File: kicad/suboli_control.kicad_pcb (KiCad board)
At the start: 2 copper layers, 125 x 95 mm, 45 parts, among them J1 DC barrel jack panel header 5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, J2 3.5 mm TRS input panel header, J4 3.5 mm TRS headphone panel he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, J5 MA12070 module power, J6 MA12070 module audio in, SW1 DPST power switch panel header, U1 TLE2426ILP

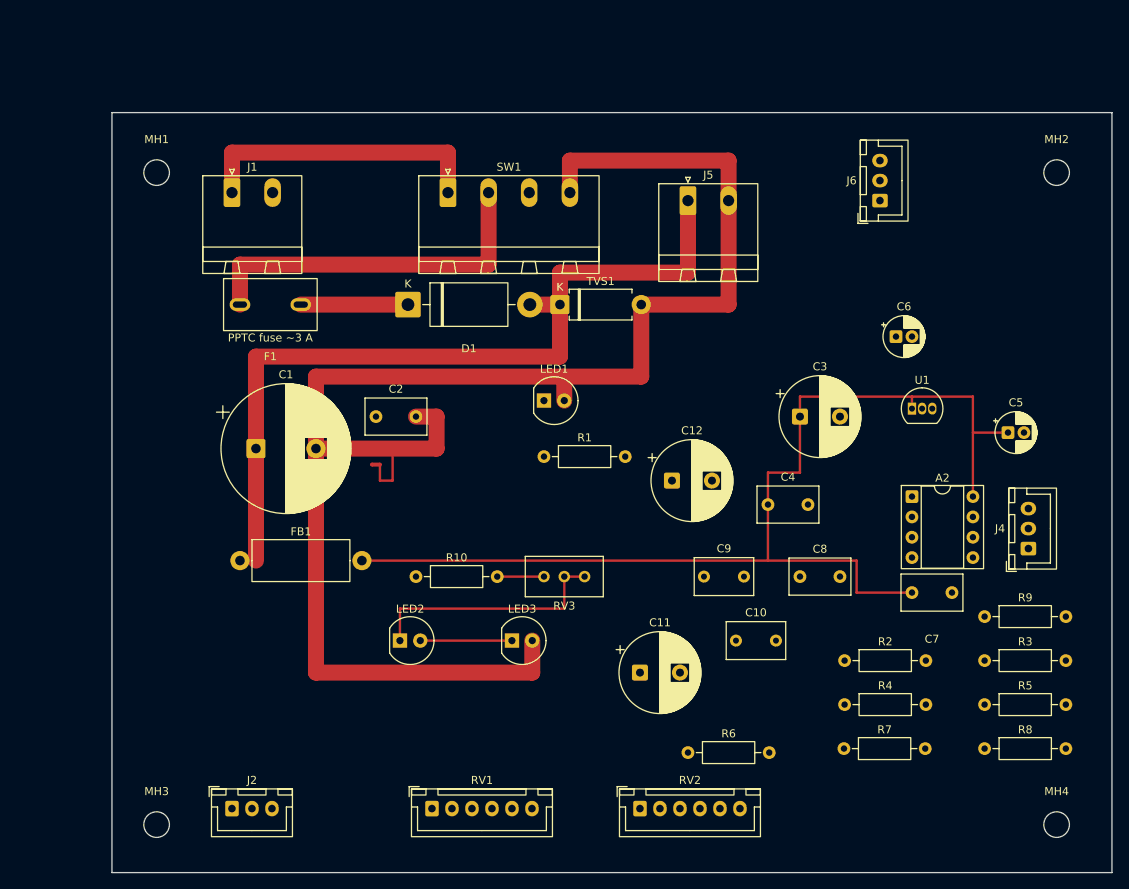
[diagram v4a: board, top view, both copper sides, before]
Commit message: R10: ground pour zones (GND_STAR left / GND_SIG right, split at x70)
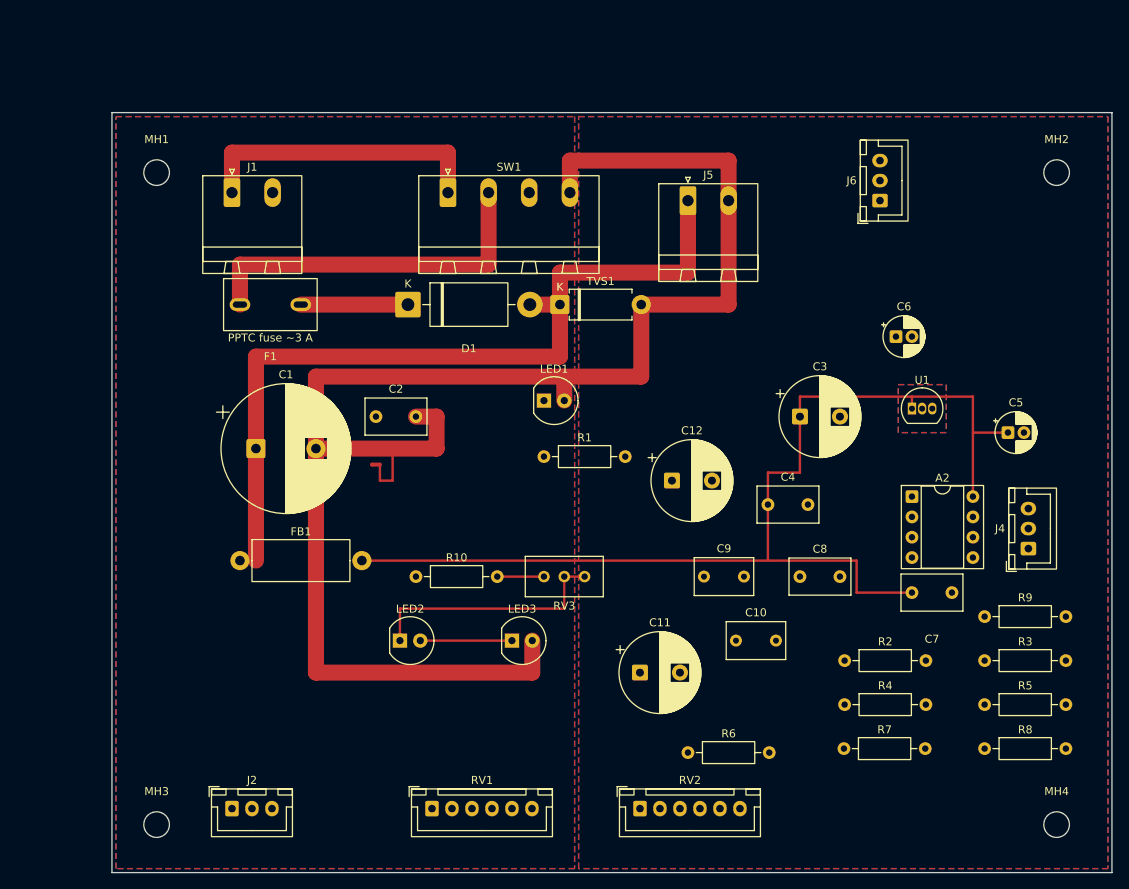
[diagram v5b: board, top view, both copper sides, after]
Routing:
- added copper zone on B.Cu, net /GND_SIG
- added copper zone on F.Cu, net /GND_SIG
- added copper zone on B.Cu, net /GND_STAR
- added copper zone on F.Cu, net /GND_STAR
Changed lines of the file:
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@@
 		(net "/+19V_F")
+	)
+	(zone
+		(net "/GND_STAR")
+		(layers "F.Cu" "B.Cu")
+		(hatch edge 0.5)
+		(connect_pads
+			(clearance 0.2)
+		)
+		(min_thickness 0.5)
+		(fill
+			(thermal_gap 0.2)
+			(thermal_bridge_width 0.5)
+			(island_removal_mode 0)
+		)
+		(polygon
+			(pts
+				(xy 12.42 12.5) (xy 69.75 12.5) (xy 69.75 106.5) (xy 12.42 106.5)
+			)
+		)
+	)
+	(zone
+		(net "/GND_SIG")
+		(layers "F.Cu" "B.Cu")
+		(hatch edge 0.5)
+		(connect_pads
+			(clearance 0.2)
+		)
+		(min_thickness 0.5)
+		(fill
+			(thermal_gap 0.2)
+			(thermal_bridge_width 0.5)
+			(island_removal_mode 0)
+		)
+		(polygon
+			(pts
+				(xy 70.25 12.5) (xy 136.42 12.5) (xy 136.42 106.5) (xy 70.25 106.5)
+			)
+		)
+		(polygon
+			(pts
+				(xy 110.2 46) (xy 116.2 46) (xy 116.2 52) (xy 110.2 52)
+			)
+		)
 	)
 	(embedded_fonts no)

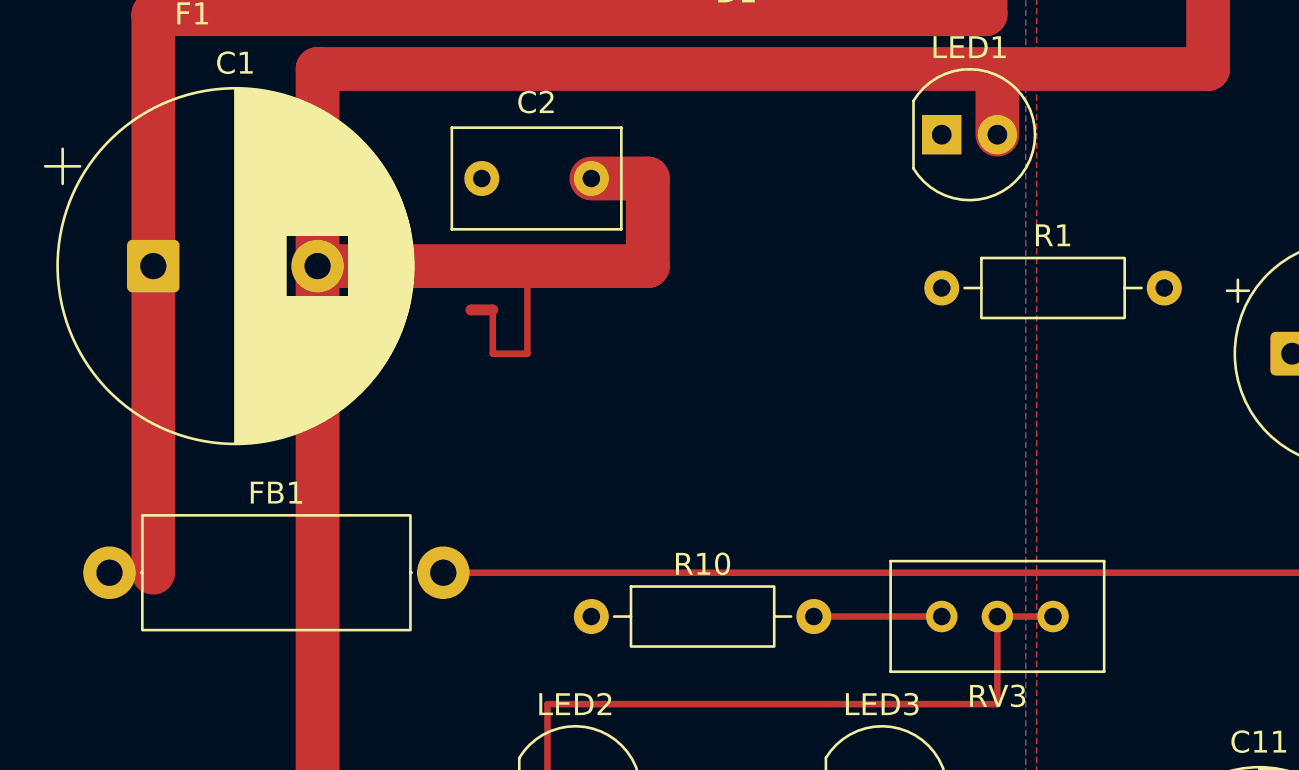
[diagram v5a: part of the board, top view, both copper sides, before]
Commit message: R11: route power leftover branches on B.Cu under ground pour
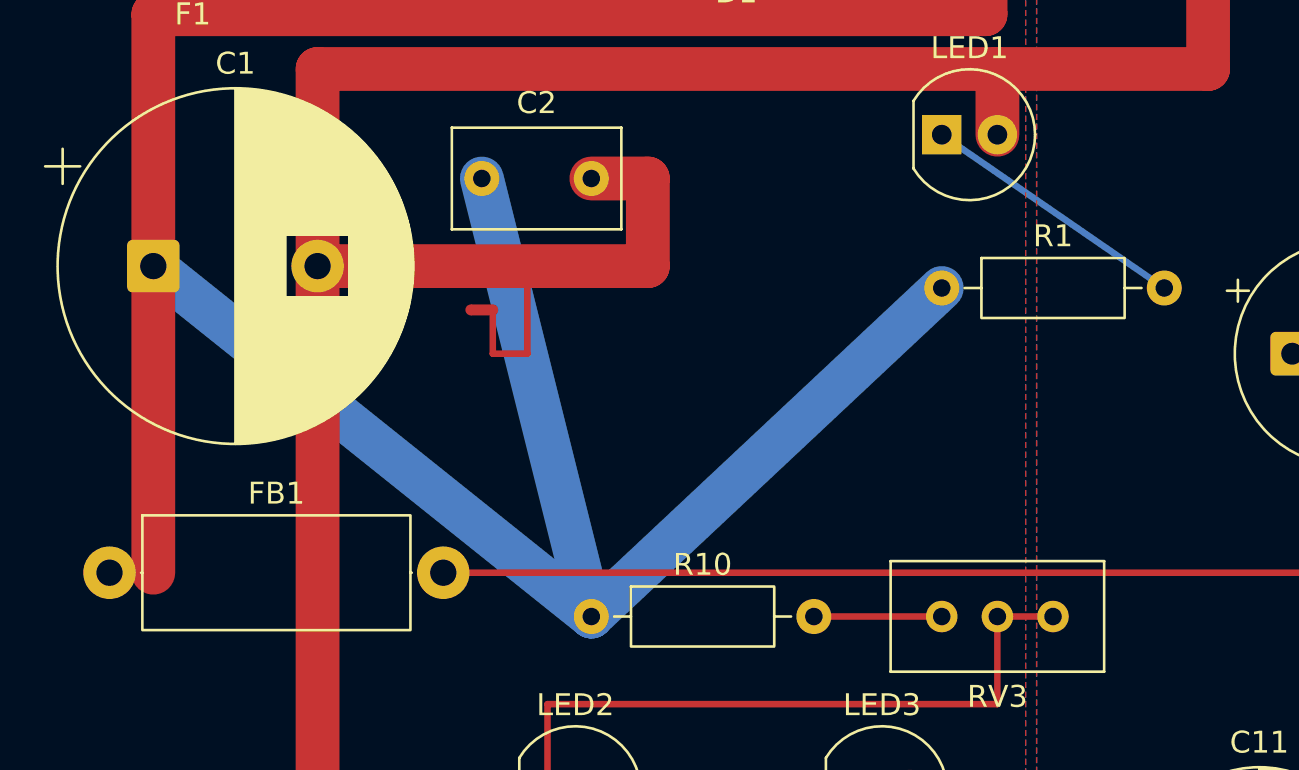
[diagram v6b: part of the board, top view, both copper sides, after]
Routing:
- net /+19V: track 102.8 -> 170.9 mm
- net /PWR_LED_ANODE: track 0.00 -> 12.3 mm
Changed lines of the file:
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@@
+	)
+	(segment
+		(start 49.92 70)
+		(end 65.92 55)
+		(width 2)
+		(layer "B.Cu")
+		(net "/+19V")
+	)
+	(segment
+		(start 29.92 54)
+		(end 49.92 70)
+		(width 2)
+		(layer "B.Cu")
+		(net "/+19V")
+	)
+	(segment
+		(start 49.92 70)
+		(end 44.92 50)
+		(width 2)
+		(layer "B.Cu")
+		(net "/+19V")
 	)
 	(segment
@@
 		(net "/+19V_F")
 	)
-	(zone
-		(net "/GND_STAR")
-		(layers "F.Cu" "B.Cu")
-		(hatch edge 0.5)
-		(connect_pads
-			(clearance 0.2)
-		)
-		(min_thickness 0.5)
-		(fill
-			(thermal_gap 0.2)
-			(thermal_bridge_width 0.5)
-			(island_removal_mode 0)
-		)
-		(polygon
-			(pts
-				(xy 12.42 12.5) (xy 69.75 12.5) (xy 69.75 106.5) (xy 12.42 106.5)
-			)
-		)
+	(segment
+		(start 65.92 48)
+		(end 76.08 55)
+		(width 0.3)
+		(layer "B.Cu")
+		(net "/PWR_LED_ANODE")
 	)
 	(zone
@@
 		)
 		(min_thickness 0.5)
-		(fill
+		(fill yes
 			(thermal_gap 0.2)
 			(thermal_bridge_width 0.5)
@@
 			)
 		)
+	)
+	(zone
+		(net "/GND_STAR")
+		(layers "F.Cu" "B.Cu")
+		(hatch edge 0.5)
+		(connect_pads
+			(clearance 0.2)
+		)
+		(min_thickness 0.5)
+		(fill yes
+			(thermal_gap 0.2)
+			(thermal_bridge_width 0.5)
+			(island_removal_mode 0)
+		)
+		(polygon
+			(pts
+				(xy 12.42 12.5) (xy 69.75 12.5) (xy 69.75 106.5) (xy 12.42 106.5)
+			)
+		)

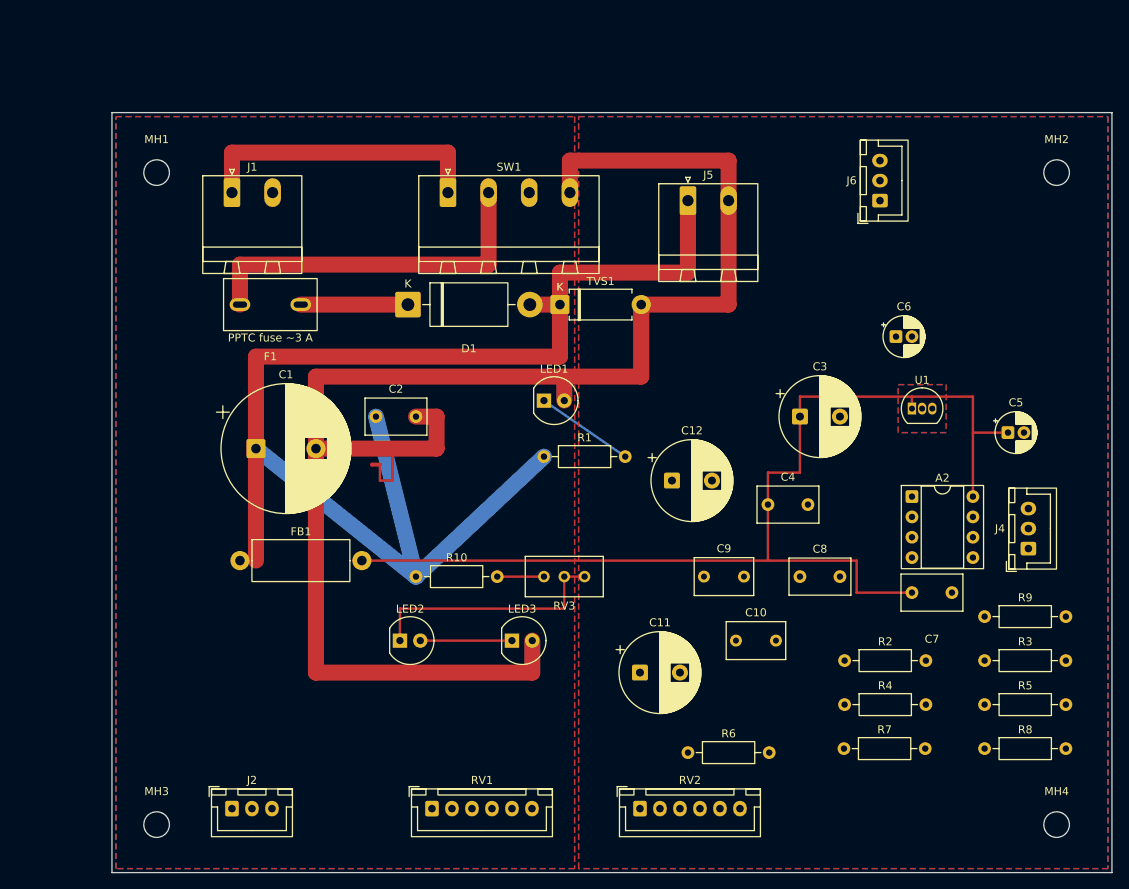
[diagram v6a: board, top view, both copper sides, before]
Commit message: R12: route input + tactile signal nets
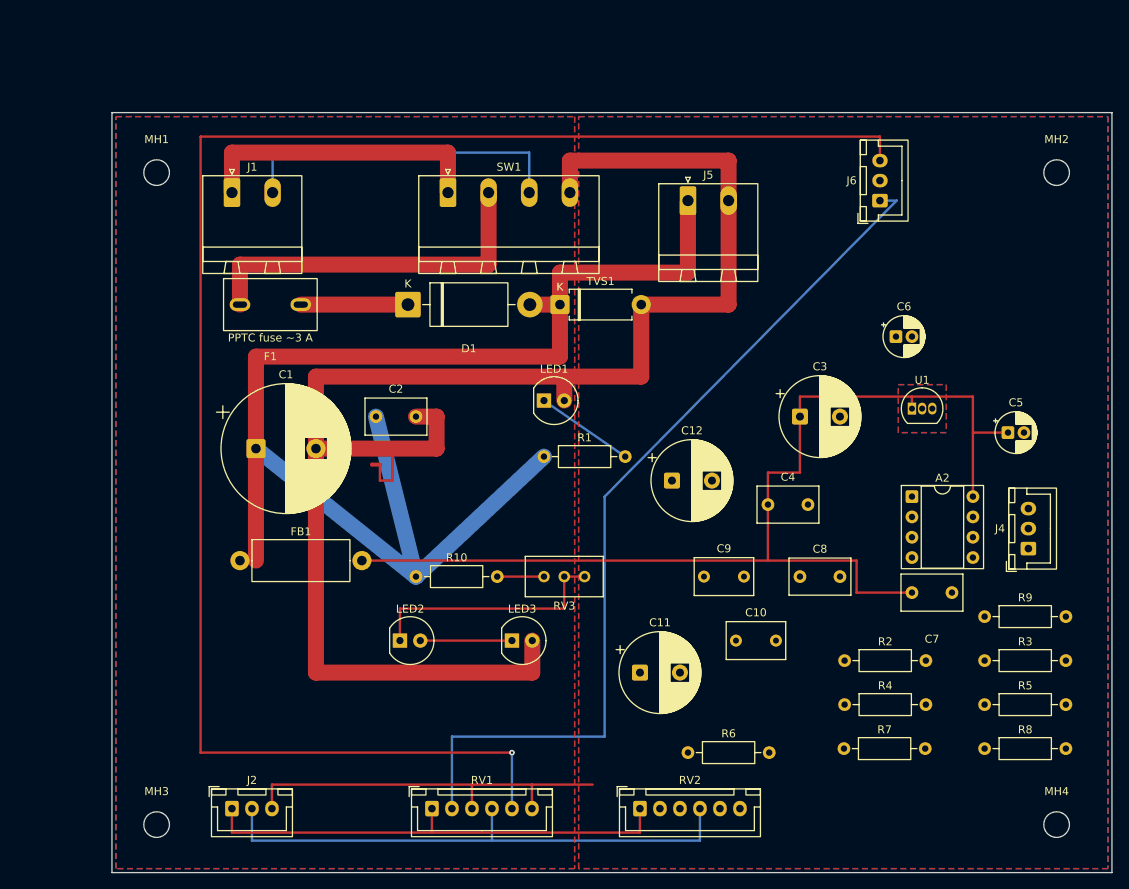
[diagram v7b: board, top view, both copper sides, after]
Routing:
- net /TACT_INR: track 0.00 -> 210.8 mm, vias 0 -> 1
- net /TACT_INL: track 0.00 -> 112.1 mm
- net /IN_R: track 0.00 -> 68.0 mm
- net /IN_L: track 0.00 -> 60.0 mm
- net /GND_SIG: track 0.00 -> 49.1 mm
- net /GND_RAW: track 0.00 -> 42.1 mm
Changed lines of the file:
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@@
+	)
+	(segment
+		(start 56.92 99)
+		(end 56.92 96)
+		(width 0.3)
+		(layer "F.Cu")
+		(net "/GND_SIG")
+	)
+	(segment
+		(start 31.92 99)
+		(end 31.92 96)
+		(width 0.3)
+		(layer "F.Cu")
+		(net "/GND_SIG")
+	)
+	(segment
+		(start 64.42 99)
+		(end 64.42 96)
+		(width 0.3)
+		(layer "F.Cu")
+		(net "/GND_SIG")
+	)
+	(segment
+		(start 31.92 96)
+		(end 72 96)
+		(width 0.3)
+		(layer "F.Cu")
+		(net "/GND_SIG")
 	)
 	(segment
@@
 	)
 	(segment
+		(start 64.08 17)
+		(end 64.08 22)
+		(width 0.3)
+		(layer "B.Cu")
+		(net "/GND_RAW")
+	)
+	(segment
+		(start 32 22)
+		(end 32 17)
+		(width 0.3)
+		(layer "B.Cu")
+		(net "/GND_RAW")
+	)
+	(segment
+		(start 32 17)
+		(end 64.08 17)
+		(width 0.3)
+		(layer "B.Cu")
+		(net "/GND_RAW")
+	)
+	(segment
 		(start 83.92 32)
 		(end 83.92 23)
@@
 	)
 	(segment
+		(start 54.42 99)
+		(end 54.42 90)
+		(width 0.3)
+		(layer "B.Cu")
+		(net "/TACT_INL")
+	)
+	(segment
+		(start 110 23)
+		(end 107.92 23)
+		(width 0.3)
+		(layer "B.Cu")
+		(net "/TACT_INL")
+	)
+	(segment
+		(start 54.42 90)
+		(end 73.5 90)
+		(width 0.3)
+		(layer "B.Cu")
+		(net "/TACT_INL")
+	)
+	(segment
+		(start 73.5 60)
+		(end 110 23)
+		(width 0.3)
+		(layer "B.Cu")
+		(net "/TACT_INL")
+	)
+	(segment
+		(start 73.5 90)
+		(end 73.5 60)
+		(width 0.3)
+		(layer "B.Cu")
+		(net "/TACT_INL")
+	)
+	(segment
+		(start 107.92 15)
+		(end 107.92 18)
+		(width 0.3)
+		(layer "F.Cu")
+		(net "/TACT_INR")
+	)
+	(segment
+		(start 61.92 92)
+		(end 23 92)
+		(width 0.3)
+		(layer "F.Cu")
+		(net "/TACT_INR")
+	)
+	(segment
+		(start 23 92)
+		(end 23 15)
+		(width 0.3)
+		(layer "F.Cu")
+		(net "/TACT_INR")
+	)
+	(segment
+		(start 23 15)
+		(end 107.92 15)
+		(width 0.3)
+		(layer "F.Cu")
+		(net "/TACT_INR")
+	)
+	(via
+		(at 61.92 92)
+		(size 0.7)
+		(drill 0.3)
+		(layers "F.Cu" "B.Cu")
+		(net "/TACT_INR")
+	)
+	(segment
+		(start 61.92 99)
+		(end 61.92 92)
+		(width 0.3)
+		(layer "B.Cu")
+		(net "/TACT_INR")
+	)
+	(segment
+		(start 77.92 99)
+		(end 77.92 102)
+		(width 0.3)
+		(layer "F.Cu")
+		(net "/IN_L")
+	)
+	(segment
+		(start 51.92 99)
+		(end 51.92 102)
+		(width 0.3)
+		(layer "F.Cu")
+		(net "/IN_L")
+	)
+	(segment
+		(start 26.92 99)
+		(end 26.92 102)
+		(width 0.3)
+		(layer "F.Cu")
+		(net "/IN_L")
+	)
+	(segment
+		(start 26.92 102)
+		(end 77.92 102)
+		(width 0.3)
+		(layer "F.Cu")
+		(net "/IN_L")
+	)
+	(segment
+		(start 85.42 99)
+		(end 85.42 103)
+		(width 0.3)
+		(layer "B.Cu")
+		(net "/IN_R")
+	)
+	(segment
+		(start 29.42 103)
+		(end 85.42 103)
+		(width 0.3)
+		(layer "B.Cu")
+		(net "/IN_R")
+	)
+	(segment
+		(start 29.42 99)
+		(end 29.42 103)
+		(width 0.3)
+		(layer "B.Cu")
+		(net "/IN_R")
+	)
+	(segment
+		(start 59.42 99)
+		(end 59.42 103)
+		(width 0.3)
+		(layer "B.Cu")
+		(net "/IN_R")
+	)
+	(segment

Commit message: R13: hand-routed analog cluster - board fully routed, 0 DRC, 0 unconnected
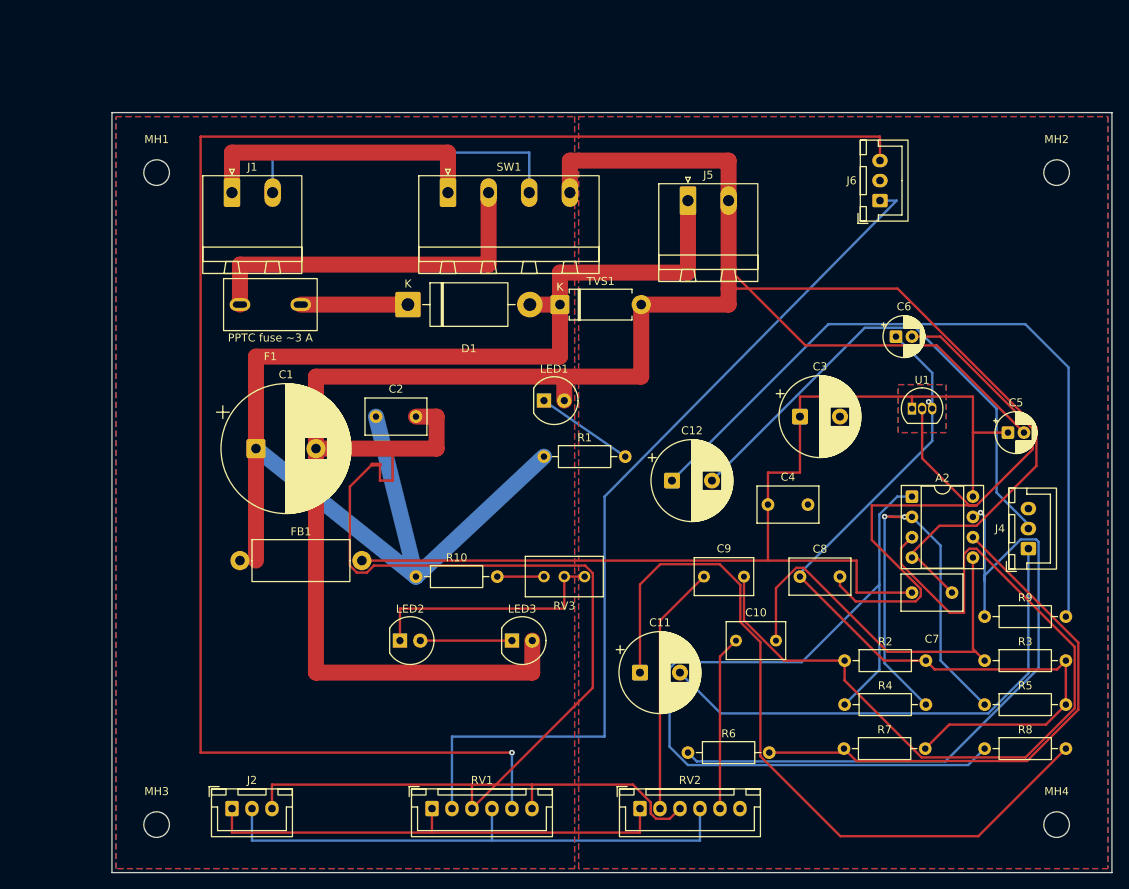
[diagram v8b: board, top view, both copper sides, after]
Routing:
- net /GND_SIG: track 49.1 -> 231.2 mm
- net /GND_STAR: track 202.7 -> 326.5 mm
- net /A2_OUT_L_RAW: track 0.00 -> 112.6 mm
- net /A2_INL_BIAS: track 0.00 -> 106.4 mm
- net /VGND: track 0.00 -> 104.2 mm, vias 0 -> 1
- net /HP_L_SER: track 0.00 -> 95.0 mm
- net /HP_R_SER: track 0.00 -> 91.2 mm
- net /A2_OUT_R_RAW: track 0.00 -> 87.5 mm, vias 0 -> 1
- net /A2_R_FB: track 0.00 -> 69.2 mm
- net /HP_OUT_R: track 0.00 -> 64.3 mm
- net /HP_OUT_L: track 0.00 -> 63.3 mm
- net /A2_L_FB: track 0.00 -> 58.8 mm, vias 0 -> 2
- net /A2_INR_BIAS: track 0.00 -> 50.4 mm
- net /HP_INL: track 0.00 -> 31.3 mm
- net /HP_INR: track 0.00 -> 21.8 mm
